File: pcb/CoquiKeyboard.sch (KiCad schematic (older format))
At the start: 116 parts

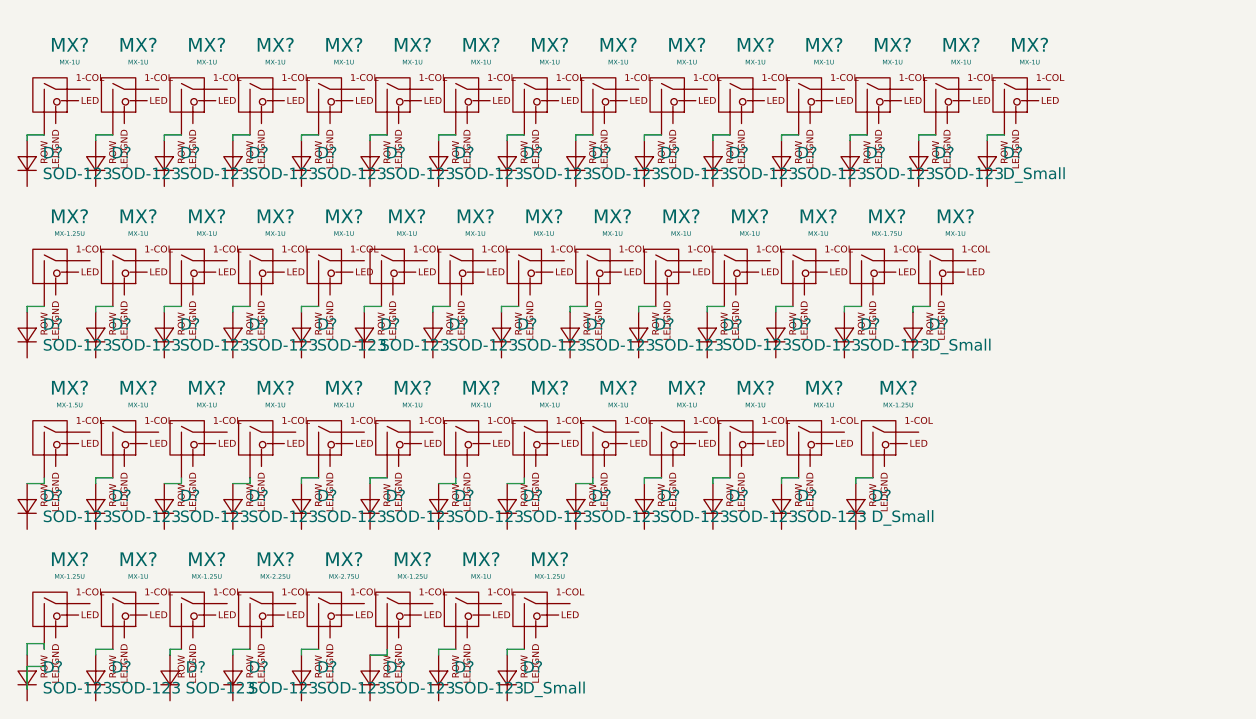
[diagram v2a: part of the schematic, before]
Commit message: realignment of switches
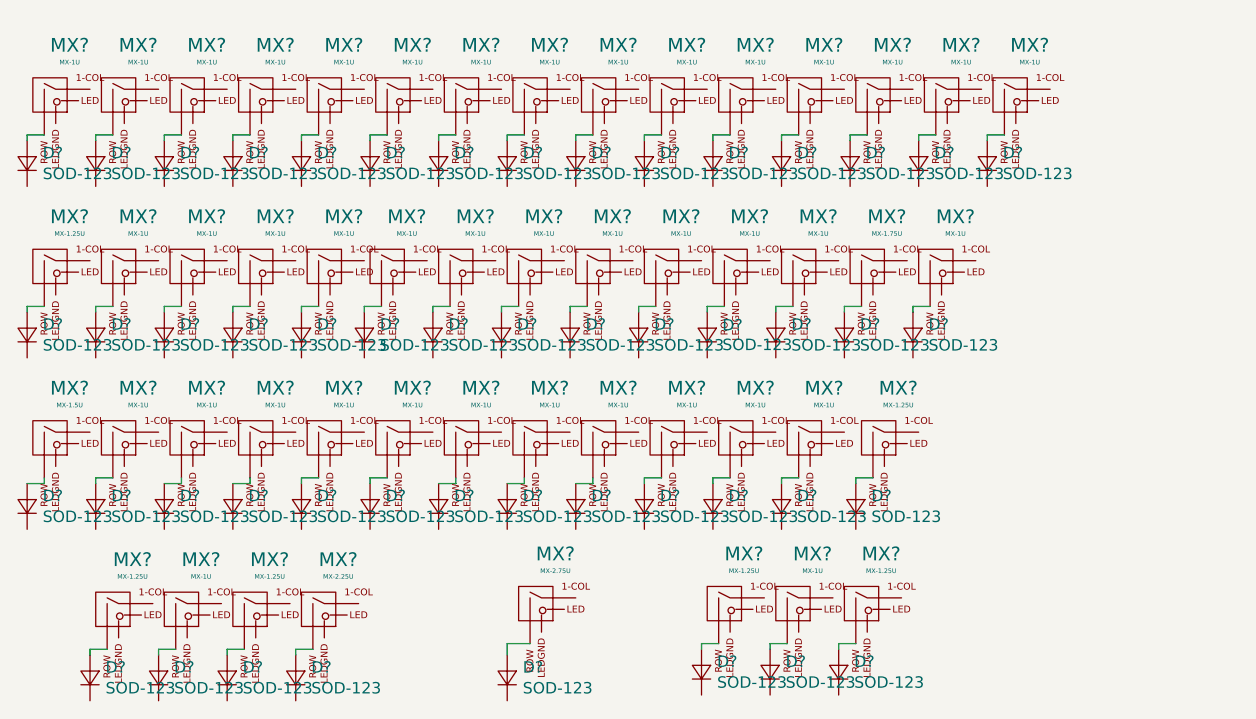
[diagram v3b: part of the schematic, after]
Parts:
- D? (x4): value D_Small -> SOD-123
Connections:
- net at MX?.2 (ROW): now also D?.2 (A); no longer D?.2 (A) (x5)
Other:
- moved on the sheet: D?, MX?
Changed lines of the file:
@@
 L MX_Alps_Hybrids:MX-1.25U MX?
 U 1 1 5CF80836
-P 1300 6600
-F 0 "MX?" H 1386 6817 60  0000 C CNN
-F 1 "MX-1.25U" H 1386 6743 20  0000 C CNN
-F 2 "" H 1275 6575 60  0001 C CNN
-F 3 "" H 1275 6575 60  0001 C CNN
-	1    1300 6600
+P 1575 6600
+F 0 "MX?" H 1661 6817 60  0000 C CNN
+F 1 "MX-1.25U" H 1661 6743 20  0000 C CNN
+F 2 "" H 1550 6575 60  0001 C CNN
+F 3 "" H 1550 6575 60  0001 C CNN
+	1    1575 6600
 	1    0    0    -1
 $EndComp
@@
 L MX_Alps_Hybrids:MX-1U MX?
 U 1 1 5CF81D4E
-P 1600 6600
-F 0 "MX?" H 1686 6817 60  0000 C CNN
-F 1 "MX-1U" H 1686 6743 20  0000 C CNN
-F 2 "" H 1575 6575 60  0001 C CNN
-F 3 "" H 1575 6575 60  0001 C CNN
-	1    1600 6600
+P 1875 6600
+F 0 "MX?" H 1961 6817 60  0000 C CNN
+F 1 "MX-1U" H 1961 6743 20  0000 C CNN
+F 2 "" H 1850 6575 60  0001 C CNN
+F 3 "" H 1850 6575 60  0001 C CNN
+	1    1875 6600
 	1    0    0    -1
 $EndComp
@@
 L MX_Alps_Hybrids:MX-1.25U MX?
 U 1 1 5CF8278E
-P 1900 6600
-F 0 "MX?" H 1986 6817 60  0000 C CNN
-F 1 "MX-1.25U" H 1986 6743 20  0000 C CNN
-F 2 "" H 1875 6575 60  0001 C CNN
-F 3 "" H 1875 6575 60  0001 C CNN
-	1    1900 6600
+P 2175 6600
+F 0 "MX?" H 2261 6817 60  0000 C CNN
+F 1 "MX-1.25U" H 2261 6743 20  0000 C CNN
+F 2 "" H 2150 6575 60  0001 C CNN
+F 3 "" H 2150 6575 60  0001 C CNN
+	1    2175 6600
 	1    0    0    -1
 $EndComp
@@
 L MX_Alps_Hybrids:MX-2.25U MX?
 U 1 1 5CF83573
-P 2200 6600
-F 0 "MX?" H 2286 6817 60  0000 C CNN
-F 1 "MX-2.25U" H 2286 6743 20  0000 C CNN
-F 2 "" H 2175 6575 60  0001 C CNN
-F 3 "" H 2175 6575 60  0001 C CNN
-	1    2200 6600
+P 2475 6600
+F 0 "MX?" H 2561 6817 60  0000 C CNN
+F 1 "MX-2.25U" H 2561 6743 20  0000 C CNN
+F 2 "" H 2450 6575 60  0001 C CNN
+F 3 "" H 2450 6575 60  0001 C CNN
+	1    2475 6600
 	1    0    0    -1
 $EndComp
@@
 L MX_Alps_Hybrids:MX-2.75U MX?
 U 1 1 5CF84597
-P 2500 6600
-F 0 "MX?" H 2586 6817 60  0000 C CNN
-F 1 "MX-2.75U" H 2586 6743 20  0000 C CNN
-F 2 "" H 2475 6575 60  0001 C CNN
-F 3 "" H 2475 6575 60  0001 C CNN
-	1    2500 6600
+P 3425 6575
+F 0 "MX?" H 3511 6792 60  0000 C CNN
+F 1 "MX-2.75U" H 3511 6718 20  0000 C CNN
+F 2 "" H 3400 6550 60  0001 C CNN
+F 3 "" H 3400 6550 60  0001 C CNN
+	1    3425 6575
 	1    0    0    -1
 $EndComp
@@
 L MX_Alps_Hybrids:MX-1.25U MX?
 U 1 1 5CF84DED
-P 2800 6600
-F 0 "MX?" H 2886 6817 60  0000 C CNN
-F 1 "MX-1.25U" H 2886 6743 20  0000 C CNN
-F 2 "" H 2775 6575 60  0001 C CNN
-F 3 "" H 2775 6575 60  0001 C CNN
-	1    2800 6600
+P 4250 6575
+F 0 "MX?" H 4336 6792 60  0000 C CNN
+F 1 "MX-1.25U" H 4336 6718 20  0000 C CNN
+F 2 "" H 4225 6550 60  0001 C CNN
+F 3 "" H 4225 6550 60  0001 C CNN
+	1    4250 6575
 	1    0    0    -1
 $EndComp
@@
 L MX_Alps_Hybrids:MX-1U MX?
 U 1 1 5CF855A2
-P 3100 6600
-F 0 "MX?" H 3186 6817 60  0000 C CNN
-F 1 "MX-1U" H 3186 6743 20  0000 C CNN
-F 2 "" H 3075 6575 60  0001 C CNN
-F 3 "" H 3075 6575 60  0001 C CNN
-	1    3100 6600
+P 4550 6575
+F 0 "MX?" H 4636 6792 60  0000 C CNN
+F 1 "MX-1U" H 4636 6718 20  0000 C CNN
+F 2 "" H 4525 6550 60  0001 C CNN
+F 3 "" H 4525 6550 60  0001 C CNN
+	1    4550 6575
 	1    0    0    -1
 $EndComp
@@
 L MX_Alps_Hybrids:MX-1.25U MX?
 U 1 1 5CF85FB0
-P 3400 6600
-F 0 "MX?" H 3486 6817 60  0000 C CNN
-F 1 "MX-1.25U" H 3486 6743 20  0000 C CNN
-F 2 "" H 3375 6575 60  0001 C CNN
-F 3 "" H 3375 6575 60  0001 C CNN
-	1    3400 6600
+P 4850 6575
+F 0 "MX?" H 4936 6792 60  0000 C CNN
+F 1 "MX-1.25U" H 4936 6718 20  0000 C CNN
+F 2 "" H 4825 6550 60  0001 C CNN
+F 3 "" H 4825 6550 60  0001 C CNN
+	1    4850 6575
 	1    0    0    -1
 $EndComp
@@
 P 5400 4650
 F 0 "D?" V 5446 4582 50  0000 R CNN
-F 1 "D_Small" V 5355 4582 50  0000 R CNN
+F 1 " SOD-123" V 5355 4582 50  0000 R CNN
 F 2 "" V 5400 4650 50  0001 C CNN
 F 3 "~" V 5400 4650 50  0001 C CNN
@@
 L Device:D_Small D?
 U 1 1 5D17B7BC
-P 1200 6900
-F 0 "D?" V 1246 6832 50  0000 R CNN
-F 1 " SOD-123" V 1155 6832 50  0000 R CNN
-F 2 "" V 1200 6900 50  0001 C CNN
-F 3 "~" V 1200 6900 50  0001 C CNN
-	1    1200 6900
+P 1475 6900
+F 0 "D?" V 1521 6832 50  0000 R CNN
+F 1 " SOD-123" V 1430 6832 50  0000 R CNN
+F 2 "" V 1475 6900 50  0001 C CNN
+F 3 "~" V 1475 6900 50  0001 C CNN
+	1    1475 6900
 	0    -1   -1   0
 $EndComp
@@
 L Device:D_Small D?
 U 1 1 5D17DCCA
-P 1500 6900
-F 0 "D?" V 1546 6832 50  0000 R CNN
-F 1 " SOD-123" V 1455 6832 50  0000 R CNN
-F 2 "" V 1500 6900 50  0001 C CNN
-F 3 "~" V 1500 6900 50  0001 C CNN
-	1    1500 6900
-	0    -1   -1   0
-$EndComp
-$Comp
-L Device:D_Small D?
-U 1 1 5D17E27A
-P 1825 6900
-F 0 "D?" V 1871 6832 50  0000 R CNN
-F 1 " SOD-123" V 1780 6832 50  0000 R CNN
-F 2 "" V 1825 6900 50  0001 C CNN
-F 3 "~" V 1825 6900 50  0001 C CNN
-	1    1825 6900
-	0    -1   -1   0
-$EndComp
-$Comp
-L Device:D_Small D?
-U 1 1 5D17ED35
-P 2100 6900
-F 0 "D?" V 2146 6832 50  0000 R CNN
-F 1 " SOD-123" V 2055 6832 50  0000 R CNN
-F 2 "" V 2100 6900 50  0001 C CNN
-F 3 "~" V 2100 6900 50  0001 C CNN
-	1    2100 6900
-	0    -1   -1   0
-$EndComp
-$Comp
-L Device:D_Small D?
-U 1 1 5D17F32B
-P 2400 6900
-F 0 "D?" V 2446 6832 50  0000 R CNN
-F 1 " SOD-123" V 2355 6832 50  0000 R CNN
-F 2 "" V 2400 6900 50  0001 C CNN
-F 3 "~" V 2400 6900 50  0001 C CNN
-	1    2400 6900
-	0    -1   -1   0
-$EndComp
-$Comp
-L Device:D_Small D?
-U 1 1 5D17FDB7
-P 2700 6900
-F 0 "D?" V 2746 6832 50  0000 R CNN
-F 1 " SOD-123" V 2655 6832 50  0000 R CNN
-F 2 "" V 2700 6900 50  0001 C CNN
-F 3 "~" V 2700 6900 50  0001 C CNN
-	1    2700 6900
-	0    -1   -1   0
-$EndComp
-$Comp
-L Device:D_Small D?
-U 1 1 5D181BC6
-P 3000 6900
-F 0 "D?" V 3046 6832 50  0000 R CNN
-F 1 " SOD-123" V 2955 6832 50  0000 R CNN
-F 2 "" V 3000 6900 50  0001 C CNN
-F 3 "~" V 3000 6900 50  0001 C CNN
-	1    3000 6900
-	0    -1   -1   0
-$EndComp
-$Comp
-L Device:D_Small D?
-U 1 1 5D1825BD
-P 3300 6900
-F 0 "D?" V 3346 6832 50  0000 R CNN
-F 1 "D_Small" V 3255 6832 50  0000 R CNN
-F 2 "" V 3300 6900 50  0001 C CNN
-F 3 "~" V 3300 6900 50  0001 C CNN
-	1    3300 6900
-	0    -1   -1   0
-$EndComp
-Wire Wire Line
-	1200 6950 1200 6850
-Wire Wire Line
-	1200 6850 1275 6850
+P 1775 6900
+F 0 "D?" V 1821 6832 50  0000 R CNN
+F 1 " SOD-123" V 1730 6832 50  0000 R CNN
+F 2 "" V 1775 6900 50  0001 C CNN
+F 3 "~" V 1775 6900 50  0001 C CNN
+	1    1775 6900
+	0    -1   -1   0
+$EndComp
 Wire Wire Line
 	4825 6050 4825 6025
 Wire Wire Line
 	4825 6025 4900 6025
-Wire Wire Line
-	2775 6800 2775 6775
 $Comp
 L Device:D_Small D?
@@
 P 4825 6150
 F 0 "D?" V 4871 6082 50  0000 R CNN
-F 1 "D_Small" V 4780 6082 50  0000 R CNN
+F 1 " SOD-123" V 4780 6082 50  0000 R CNN
 F 2 "" V 4825 6150 50  0001 C CNN
 F 3 "~" V 4825 6150 50  0001 C CNN
@@
 P 5075 5400
 F 0 "D?" V 5121 5332 50  0000 R CNN
-F 1 "D_Small" V 5030 5332 50  0000 R CNN
+F 1 " SOD-123" V 5030 5332 50  0000 R CNN
 F 2 "" V 5075 5400 50  0001 C CNN
 F 3 "~" V 5075 5400 50  0001 C CNN
@@
 $EndComp
 Wire Wire Line
-	2700 6800 2775 6800
-Wire Wire Line
 	1200 6050 1275 6050
 Wire Wire Line
@@
 	3900 4525 3900 4550
 Wire Wire Line
-	1200 6800 1200 6750
-Wire Wire Line
-	1200 6750 1275 6750
-Wire Wire Line
-	1275 6750 1275 6775
-Wire Wire Line
-	1500 6800 1500 6775
-Wire Wire Line
-	1500 6775 1575 6775
-Wire Wire Line
-	1825 6800 1825 6775
-Wire Wire Line
-	1825 6775 1875 6775
-Wire Wire Line
-	2100 6800 2100 6775
-Wire Wire Line
-	2100 6775 2175 6775
-Wire Wire Line
-	2400 6800 2400 6775
-Wire Wire Line
-	2400 6775 2475 6775
-Wire Wire Line
-	3000 6800 3000 6775
-Wire Wire Line
-	3000 6775 3075 6775
-Wire Wire Line
-	3300 6800 3300 6775
-Wire Wire Line
-	3300 6775 3375 6775
+	1775 6800 1775 6775
+Wire Wire Line
+	1775 6775 1850 6775
 Wire Wire Line
 	2100 5300 2100 5275
@@
 Wire Wire Line
 	2400 6025 2475 6025
+Wire Wire Line
+	1475 6800 1475 6775
+Wire Wire Line
+	1475 6775 1550 6775
+$Comp
+L Device:D_Small D?
+U 1 1 5D1825BD
+P 4450 6875
+F 0 "D?" V 4496 6807 50  0000 R CNN
+F 1 " SOD-123" V 4405 6807 50  0000 R CNN
+F 2 "" V 4450 6875 50  0001 C CNN
+F 3 "~" V 4450 6875 50  0001 C CNN
+	1    4450 6875
+	0    -1   -1   0
+$EndComp
+$Comp
+L Device:D_Small D?
+U 1 1 5D181BC6
+P 4150 6875
+F 0 "D?" V 4196 6807 50  0000 R CNN
+F 1 " SOD-123" V 4105 6807 50  0000 R CNN
+F 2 "" V 4150 6875 50  0001 C CNN
+F 3 "~" V 4150 6875 50  0001 C CNN
+	1    4150 6875
+	0    -1   -1   0
+$EndComp
+$Comp
+L Device:D_Small D?
+U 1 1 5D17FDB7
+P 3300 6900
+F 0 "D?" V 3346 6832 50  0000 R CNN
+F 1 " SOD-123" V 3255 6832 50  0000 R CNN
+F 2 "" V 3300 6900 50  0001 C CNN
+F 3 "~" V 3300 6900 50  0001 C CNN
+	1    3300 6900
+	0    -1   -1   0
+$EndComp
+$Comp
+L Device:D_Small D?
+U 1 1 5D17F32B
+P 2375 6900
+F 0 "D?" V 2421 6832 50  0000 R CNN
+F 1 " SOD-123" V 2330 6832 50  0000 R CNN
+F 2 "" V 2375 6900 50  0001 C CNN
+F 3 "~" V 2375 6900 50  0001 C CNN
+	1    2375 6900
+	0    -1   -1   0
+$EndComp
+$Comp
+L Device:D_Small D?
+U 1 1 5D17ED35
+P 4750 6875
+F 0 "D?" V 4796 6807 50  0000 R CNN
+F 1 " SOD-123" V 4705 6807 50  0000 R CNN
+F 2 "" V 4750 6875 50  0001 C CNN
+F 3 "~" V 4750 6875 50  0001 C CNN
+	1    4750 6875
+	0    -1   -1   0
+$EndComp
+Wire Wire Line
+	2375 6800 2375 6775
+Wire Wire Line
+	2375 6775 2450 6775
+$Comp
+L Device:D_Small D?
+U 1 1 5D17E27A
+P 2075 6900
+F 0 "D?" V 2121 6832 50  0000 R CNN
+F 1 " SOD-123" V 2030 6832 50  0000 R CNN
+F 2 "" V 2075 6900 50  0001 C CNN
+F 3 "~" V 2075 6900 50  0001 C CNN
+	1    2075 6900
+	0    -1   -1   0
+$EndComp
+Wire Wire Line
+	2075 6800 2075 6775
+Wire Wire Line
+	2075 6775 2150 6775
+Wire Wire Line
+	3300 6800 3300 6750
+Wire Wire Line
+	3300 6750 3400 6750
+Wire Wire Line
+	4150 6775 4150 6750
+Wire Wire Line
+	4150 6750 4225 6750
+Wire Wire Line
+	4450 6775 4450 6750
+Wire Wire Line
+	4450 6750 4525 6750
+Wire Wire Line
+	4750 6775 4750 6750
+Wire Wire Line
+	4750 6750 4825 6750
 $EndSCHEMATC

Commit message: draw matrices
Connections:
- wire segments 149 -> 246
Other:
- moved on the sheet: D?, MX?

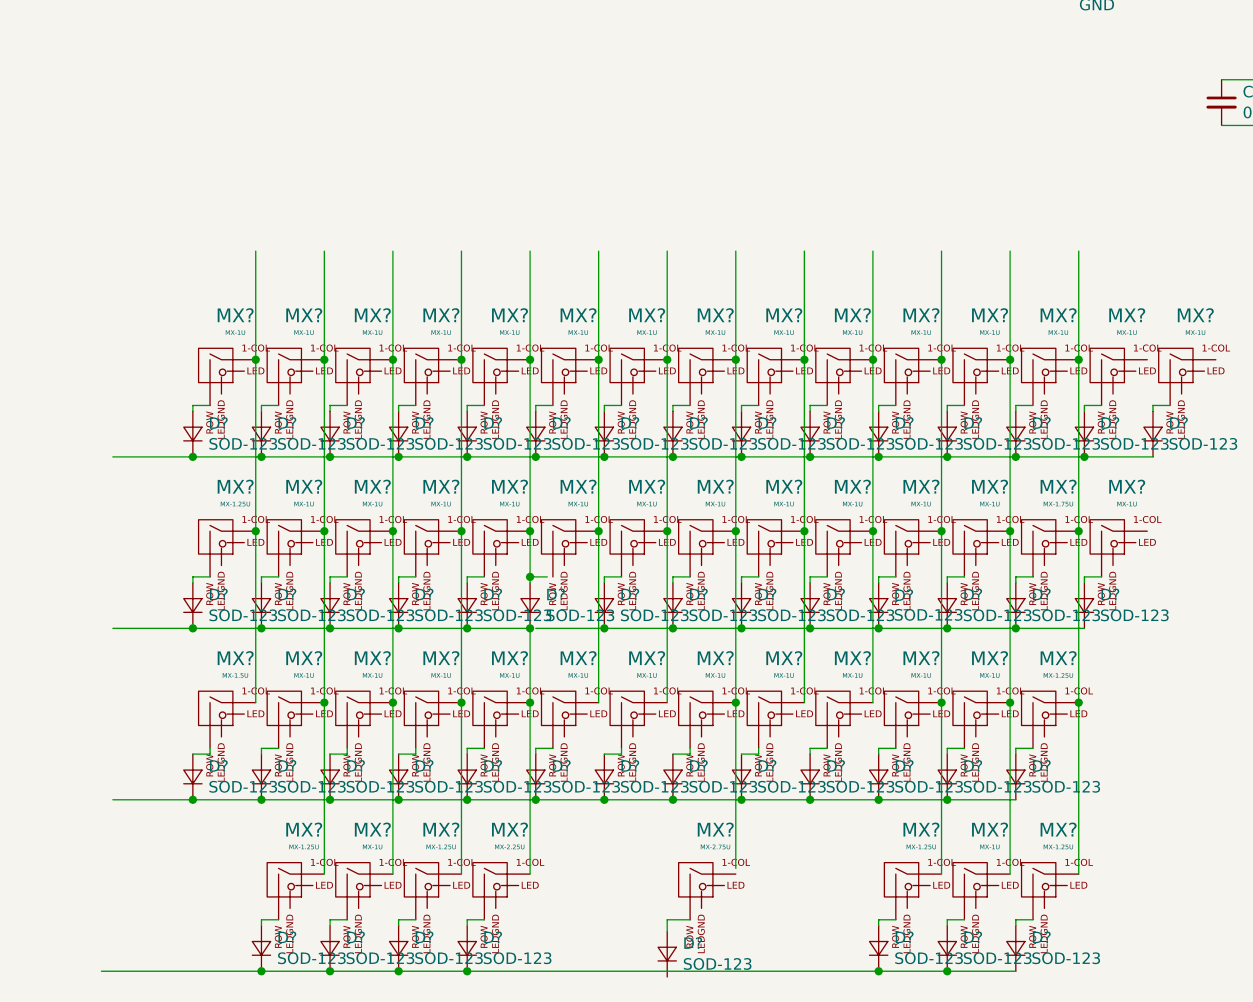
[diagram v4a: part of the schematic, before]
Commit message: label matrix
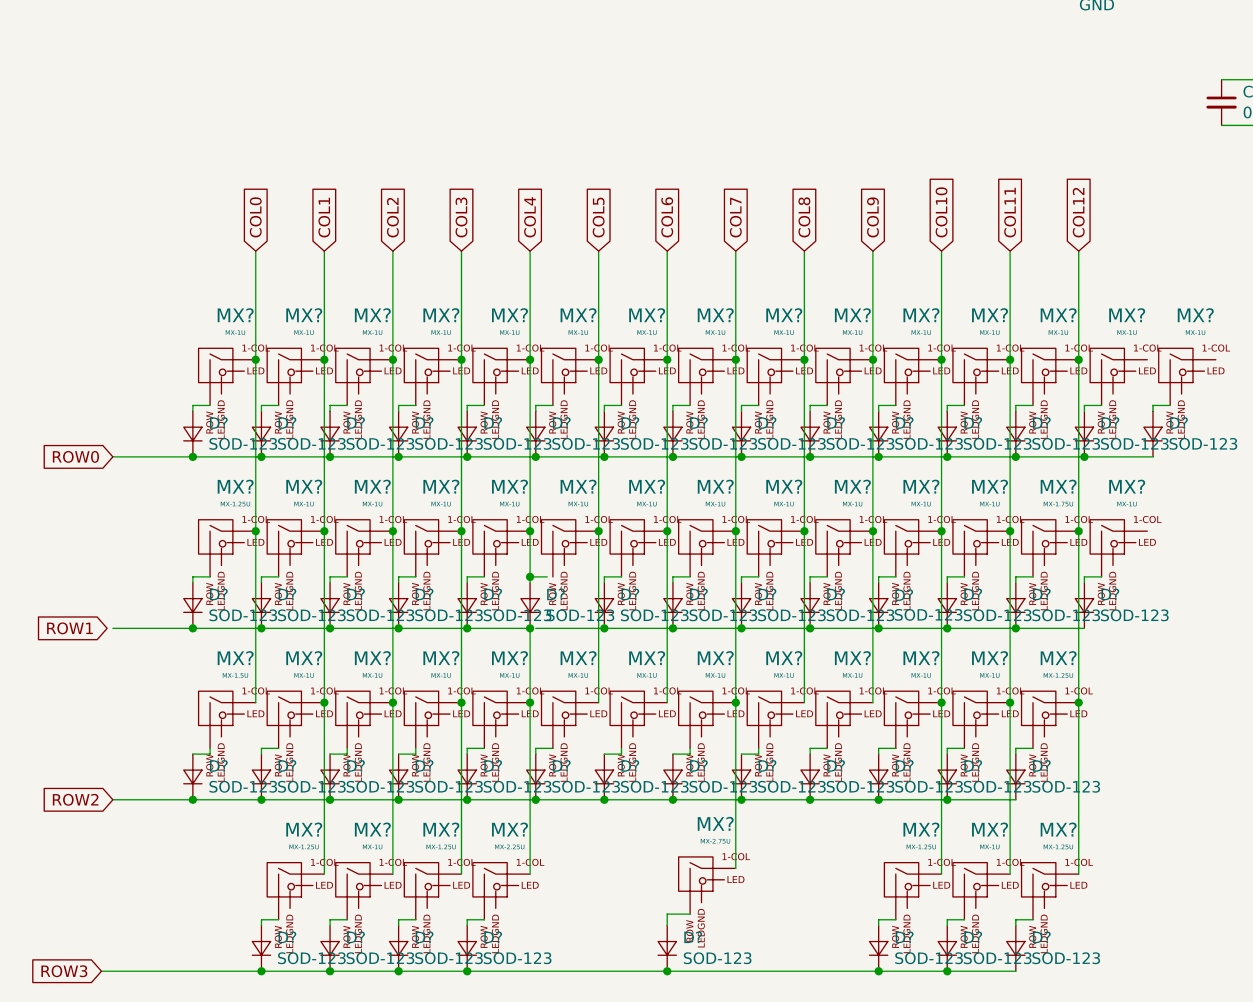
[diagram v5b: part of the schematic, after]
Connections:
- net labels added: COL0, COL1, COL10, COL11, COL12, COL2, COL3, COL4, COL5, COL6, COL7, COL8, COL9, ROW0, ROW1, ROW2, ROW3
- wire segments 246 -> 248
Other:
- moved on the sheet: D?, MX?
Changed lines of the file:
@@
 L MX_Alps_Hybrids:MX-2.75U MX?
 U 1 1 5CF84597
-P 3400 6600
-F 0 "MX?" H 3486 6817 60  0000 C CNN
-F 1 "MX-2.75U" H 3486 6743 20  0000 C CNN
-F 2 "" H 3375 6575 60  0001 C CNN
-F 3 "" H 3375 6575 60  0001 C CNN
-	1    3400 6600
+P 3400 6575
+F 0 "MX?" H 3486 6792 60  0000 C CNN
+F 1 "MX-2.75U" H 3486 6718 20  0000 C CNN
+F 2 "" H 3375 6550 60  0001 C CNN
+F 3 "" H 3375 6550 60  0001 C CNN
+	1    3400 6575
 	1    0    0    -1
 $EndComp
@@
 L Device:D_Small D?
 U 1 1 5D17FDB7
-P 3275 6925
-F 0 "D?" V 3321 6857 50  0000 R CNN
-F 1 " SOD-123" V 3230 6857 50  0000 R CNN
-F 2 "" V 3275 6925 50  0001 C CNN
-F 3 "~" V 3275 6925 50  0001 C CNN
-	1    3275 6925
+P 3275 6900
+F 0 "D?" V 3321 6832 50  0000 R CNN
+F 1 " SOD-123" V 3230 6832 50  0000 R CNN
+F 2 "" V 3275 6900 50  0001 C CNN
+F 3 "~" V 3275 6900 50  0001 C CNN
+	1    3275 6900
 	0    -1   -1   0
 $EndComp
@@
 	2100 6775 2175 6775
 Wire Wire Line
-	3275 6825 3275 6775
-Wire Wire Line
-	3275 6775 3375 6775
+	3275 6800 3275 6750
+Wire Wire Line
+	3275 6750 3375 6750
 Wire Wire Line
 	4200 6800 4200 6775
@@
 Wire Wire Line
 	2100 7000 2400 7000
-Connection ~ 2400 7000
-Wire Wire Line
-	2400 7000 4200 7000
-Connection ~ 4200 7000
 Wire Wire Line
 	4200 7000 4500 7000
@@
 Wire Wire Line
 	4500 7000 4800 7000
-Wire Wire Line
-	3575 6550 3575 5825
 Connection ~ 3575 4325
 Wire Wire Line
@@
 Connection ~ 3575 5825
 Wire Wire Line
-	3575 5825 3575 5075
-Wire Wire Line
 	3875 5825 3875 5075
 Connection ~ 3875 4325
@@
 	3275 4325 3275 3850
 Connection ~ 3275 4325
+Text GLabel 1475 3850 1    50   Input ~ 0
+COL0
+Text GLabel 1775 3850 1    50   Input ~ 0
+COL1
+Text GLabel 2075 3850 1    50   Input ~ 0
+COL2
+Text GLabel 2675 3850 1    50   Input ~ 0
+COL4
+Text GLabel 2375 3850 1    50   Input ~ 0
+COL3
+Text GLabel 2975 3850 1    50   Input ~ 0
+COL5
+Text GLabel 3275 3850 1    50   Input ~ 0
+COL6
+Text GLabel 3575 3850 1    50   Input ~ 0
+COL7
+Text GLabel 3875 3850 1    50   Input ~ 0
+COL8
+Text GLabel 4175 3850 1    50   Input ~ 0
+COL9
+Text GLabel 4475 3850 1    50   Input ~ 0
+COL10
+Text GLabel 4775 3850 1    50   Input ~ 0
+COL11
+Text GLabel 5075 3850 1    50   Input ~ 0
+COL12
+Text GLabel 825  5500 0    50   Input ~ 0
+ROW1
+Text GLabel 850  4750 0    50   Input ~ 0
+ROW0
+Text GLabel 850  6250 0    50   Input ~ 0
+ROW2
+Text GLabel 800  7000 0    50   Input ~ 0
+ROW3
+Wire Wire Line
+	2400 7000 3275 7000
+Wire Wire Line
+	3575 5800 3575 5825
+Wire Wire Line
+	3575 5075 3575 5825
+Connection ~ 2400 7000
+Connection ~ 4200 7000
+Connection ~ 3275 7000
+Wire Wire Line
+	3275 7000 4200 7000
+Wire Wire Line
+	3575 5825 3575 6550
 $EndSCHEMATC
